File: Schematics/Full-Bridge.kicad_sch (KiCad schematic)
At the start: 3 parts, among them J14 464379202, J15 464369202, J9 43650-0418

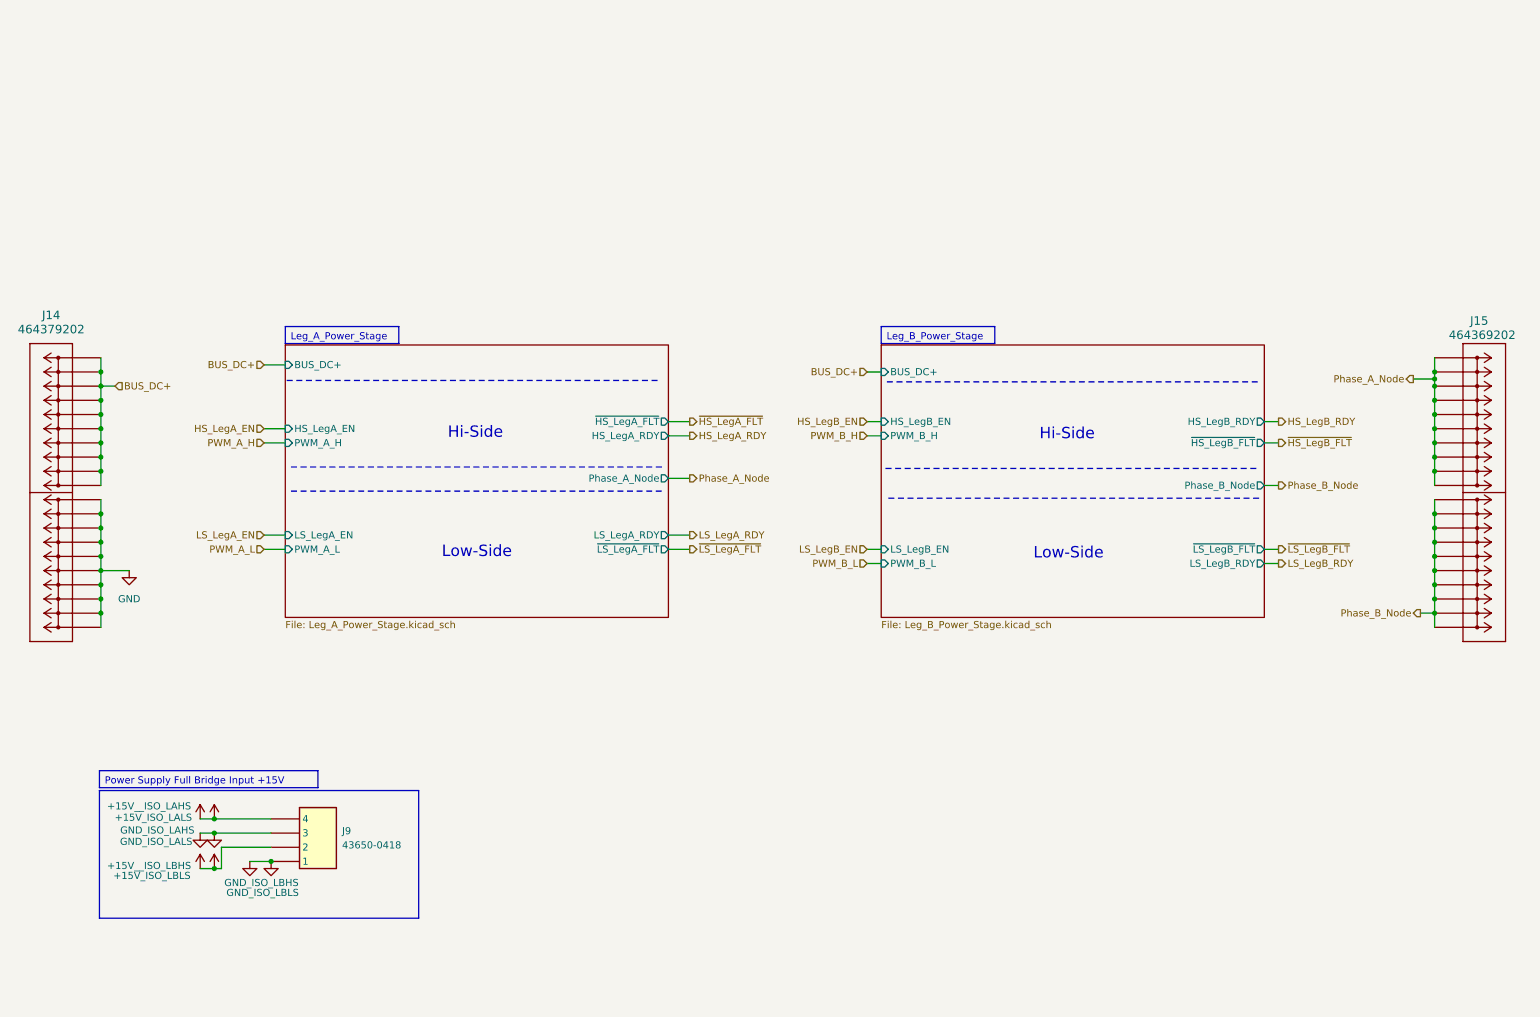
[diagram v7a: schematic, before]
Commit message: [WIP Single Phase Inverter]
- Changed all Refs within each sub sheet (Stripe)
- Added 3V3 Power Supply off of 15V iso supply
- Added footprint, symbol and 3d part
- updated PCB with new part
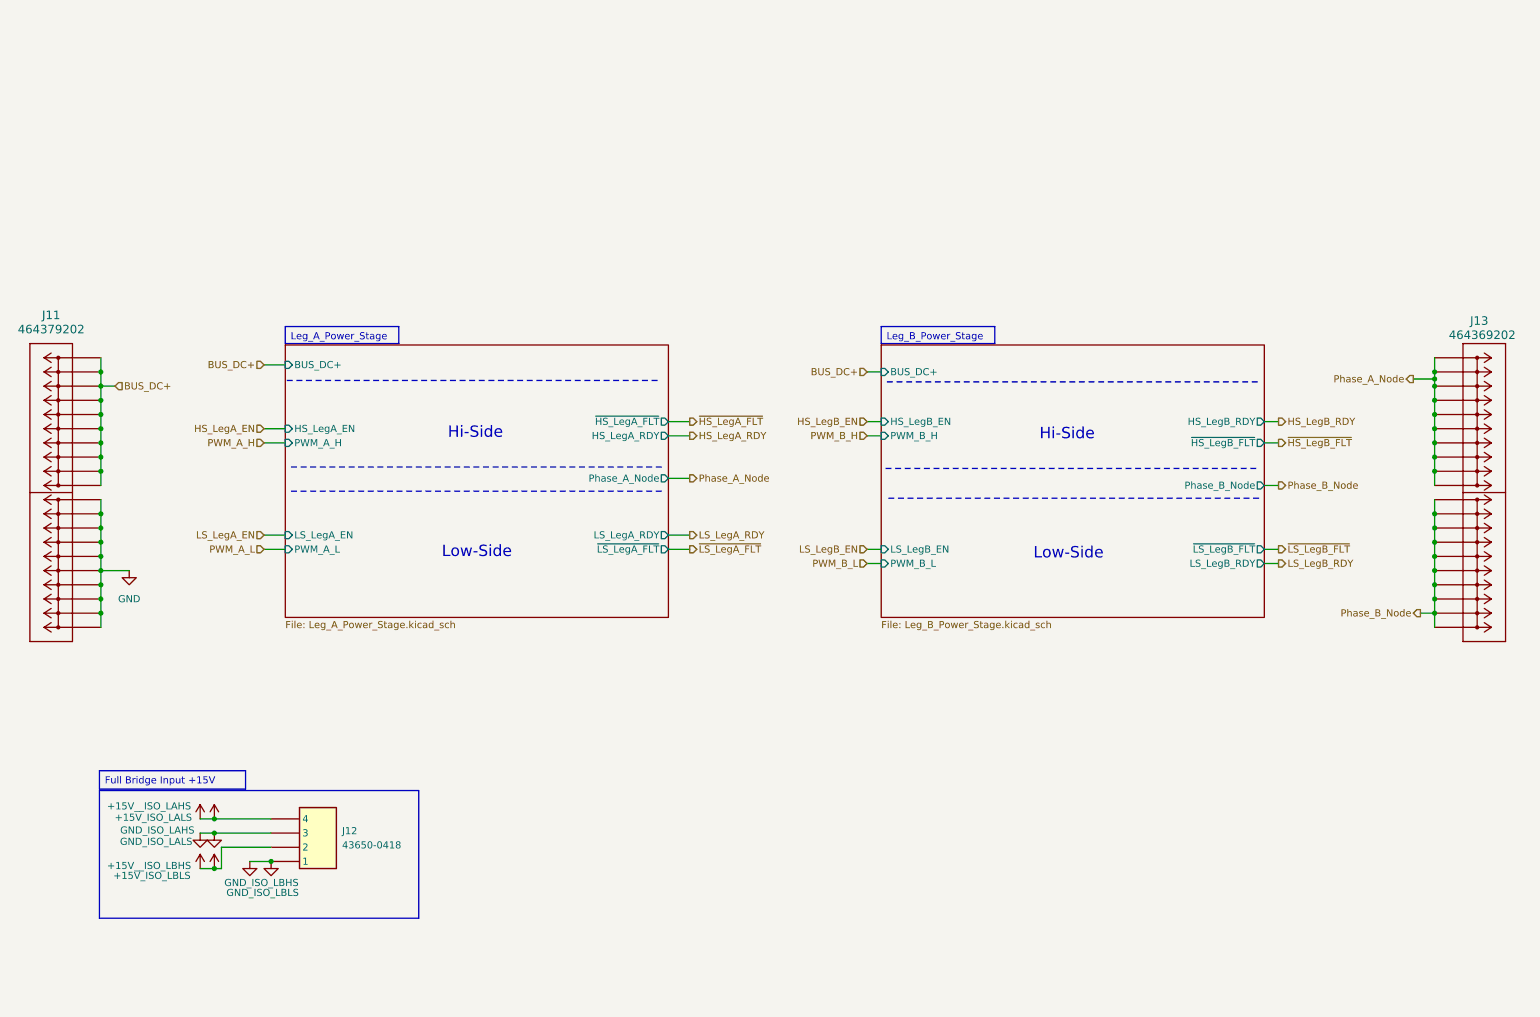
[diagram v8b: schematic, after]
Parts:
- renumbered J14 to J11, J9 to J12, J15 to J13
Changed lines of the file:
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@@
 		)
 	)
-	(text_box "Power Supply Full Bridge Input +15V"
+	(text_box "Full Bridge Input +15V"
 		(exclude_from_sim no)
 		(at 28.956 151.384 0)
-		(size 39.116 3.048)
+		(size 26.162 3.302)
 		(margins 0.9525 0.9525 0.9525 0.9525)
 		(stroke
@@
 		(on_board yes)
 		(dnp no)
-		(property "Reference" "J15"
+		(property "Reference" "J13"
 			(at 274.32 70.866 0)
 			(effects
@@
 			(project "SiC_Single_Phase_Inverter"
 				(path "/a1ed0539-9735-4ad1-a8fd-87e26e7fce16/b6e78e1f-718a-4f31-892b-d9c389541b0d"
-					(reference "J15")
+					(reference "J13")
 					(unit 1)
 				)
@@
 		(on_board yes)
 		(dnp no)
-		(property "Reference" "#PWR083"
+		(property "Reference" "#PWR018"
 			(at 55.88 173.99 0)
 			(effects
@@
 			(project "SiC_Single_Phase_Inverter"
 				(path "/a1ed0539-9735-4ad1-a8fd-87e26e7fce16/b6e78e1f-718a-4f31-892b-d9c389541b0d"
-					(reference "#PWR083")
+					(reference "#PWR018")
 					(unit 1)
 				)
@@
 		(dnp no)
 		(fields_autoplaced yes)
-		(property "Reference" "J14"
+		(property "Reference" "J11"
 			(at 20.32 69.85 0)
 			(effects
@@
 			(project "SiC_Single_Phase_Inverter"
 				(path "/a1ed0539-9735-4ad1-a8fd-87e26e7fce16/b6e78e1f-718a-4f31-892b-d9c389541b0d"
-					(reference "J14")
+					(reference "J11")
 					(unit 1)
 				)
@@
 		(on_board yes)
 		(dnp no)
-		(property "Reference" "#PWR082"
+		(property "Reference" "#PWR017"
 			(at 49.53 172.72 0)
 			(effects
@@
 			(project "SiC_Single_Phase_Inverter"
 				(path "/a1ed0539-9735-4ad1-a8fd-87e26e7fce16/b6e78e1f-718a-4f31-892b-d9c389541b0d"
-					(reference "#PWR082")
+					(reference "#PWR017")
 					(unit 1)
 				)
@@
 		(on_board yes)
 		(dnp no)
-		(property "Reference" "#PWR072"
+		(property "Reference" "#PWR014"
 			(at 46.99 172.72 0)
 			(effects
@@
 			(project "SiC_Single_Phase_Inverter"
 				(path "/a1ed0539-9735-4ad1-a8fd-87e26e7fce16/b6e78e1f-718a-4f31-892b-d9c389541b0d"
-					(reference "#PWR072")
+					(reference "#PWR014")
 					(unit 1)
 				)
@@
 		(on_board yes)
 		(dnp no)
-		(property "Reference" "#PWR086"
+		(property "Reference" "#PWR015"
 			(at 49.53 163.83 0)
 			(effects
@@
 			(project "SiC_Single_Phase_Inverter"
 				(path "/a1ed0539-9735-4ad1-a8fd-87e26e7fce16/b6e78e1f-718a-4f31-892b-d9c389541b0d"
-					(reference "#PWR086")
+					(reference "#PWR015")
 					(unit 1)
 				)
@@
 		(on_board yes)
 		(dnp no)
-		(property "Reference" "#PWR073"
+		(property "Reference" "#PWR019"
 			(at 59.69 173.99 0)
 			(effects
@@
 			(project "SiC_Single_Phase_Inverter"
 				(path "/a1ed0539-9735-4ad1-a8fd-87e26e7fce16/b6e78e1f-718a-4f31-892b-d9c389541b0d"
-					(reference "#PWR073")
+					(reference "#PWR019")
 					(unit 1)
 				)
@@
 		(on_board yes)
 		(dnp no)
-		(property "Reference" "#PWR087"
+		(property "Reference" "#PWR016"
 			(at 49.53 168.91 0)
 			(effects
@@
 			(project "SiC_Single_Phase_Inverter"
 				(path "/a1ed0539-9735-4ad1-a8fd-87e26e7fce16/b6e78e1f-718a-4f31-892b-d9c389541b0d"
-					(reference "#PWR087")
+					(reference "#PWR016")
 					(unit 1)
 				)
@@
 		(dnp no)
 		(fields_autoplaced yes)
-		(property "Reference" "#PWR092"
+		(property "Reference" "#PWR011"
 			(at 34.29 121.92 0)
 			(effects
@@
 			(project "SiC_Single_Phase_Inverter"
 				(path "/a1ed0539-9735-4ad1-a8fd-87e26e7fce16/b6e78e1f-718a-4f31-892b-d9c389541b0d"
-					(reference "#PWR092")
+					(reference "#PWR011")
 					(unit 1)
 				)
@@
 		(dnp no)
 		(fields_autoplaced yes)
-		(property "Reference" "J9"
+		(property "Reference" "J12"
 			(at 72.39 162.1789 0)
 			(effects
@@
 			(project "SiC_Single_Phase_Inverter"
 				(path "/a1ed0539-9735-4ad1-a8fd-87e26e7fce16/b6e78e1f-718a-4f31-892b-d9c389541b0d"
-					(reference "J9")
+					(reference "J12")
 					(unit 1)
 				)
@@
 		(on_board yes)
 		(dnp no)
-		(property "Reference" "#PWR084"
+		(property "Reference" "#PWR012"
 			(at 46.99 163.83 0)
 			(effects
@@
 			(project "SiC_Single_Phase_Inverter"
 				(path "/a1ed0539-9735-4ad1-a8fd-87e26e7fce16/b6e78e1f-718a-4f31-892b-d9c389541b0d"
-					(reference "#PWR084")
+					(reference "#PWR012")
 					(unit 1)
 				)
@@
 		(on_board yes)
 		(dnp no)
-		(property "Reference" "#PWR085"
+		(property "Reference" "#PWR013"
 			(at 46.99 168.91 0)
 			(effects
@@
 			(project "SiC_Single_Phase_Inverter"
 				(path "/a1ed0539-9735-4ad1-a8fd-87e26e7fce16/b6e78e1f-718a-4f31-892b-d9c389541b0d"
-					(reference "#PWR085")
+					(reference "#PWR013")
 					(unit 1)
 				)
